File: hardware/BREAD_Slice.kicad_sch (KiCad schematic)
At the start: 23 parts, among them J1 I2C_01x04, J2 Conn_01x10_Female, J3 Screw_Terminal_01x02, J4 Screw_Terminal_01x02, J5 Screw_Terminal_01x06, J6 Screw_Terminal_01x06, SW1 ESTOP, SW2 ESTOP

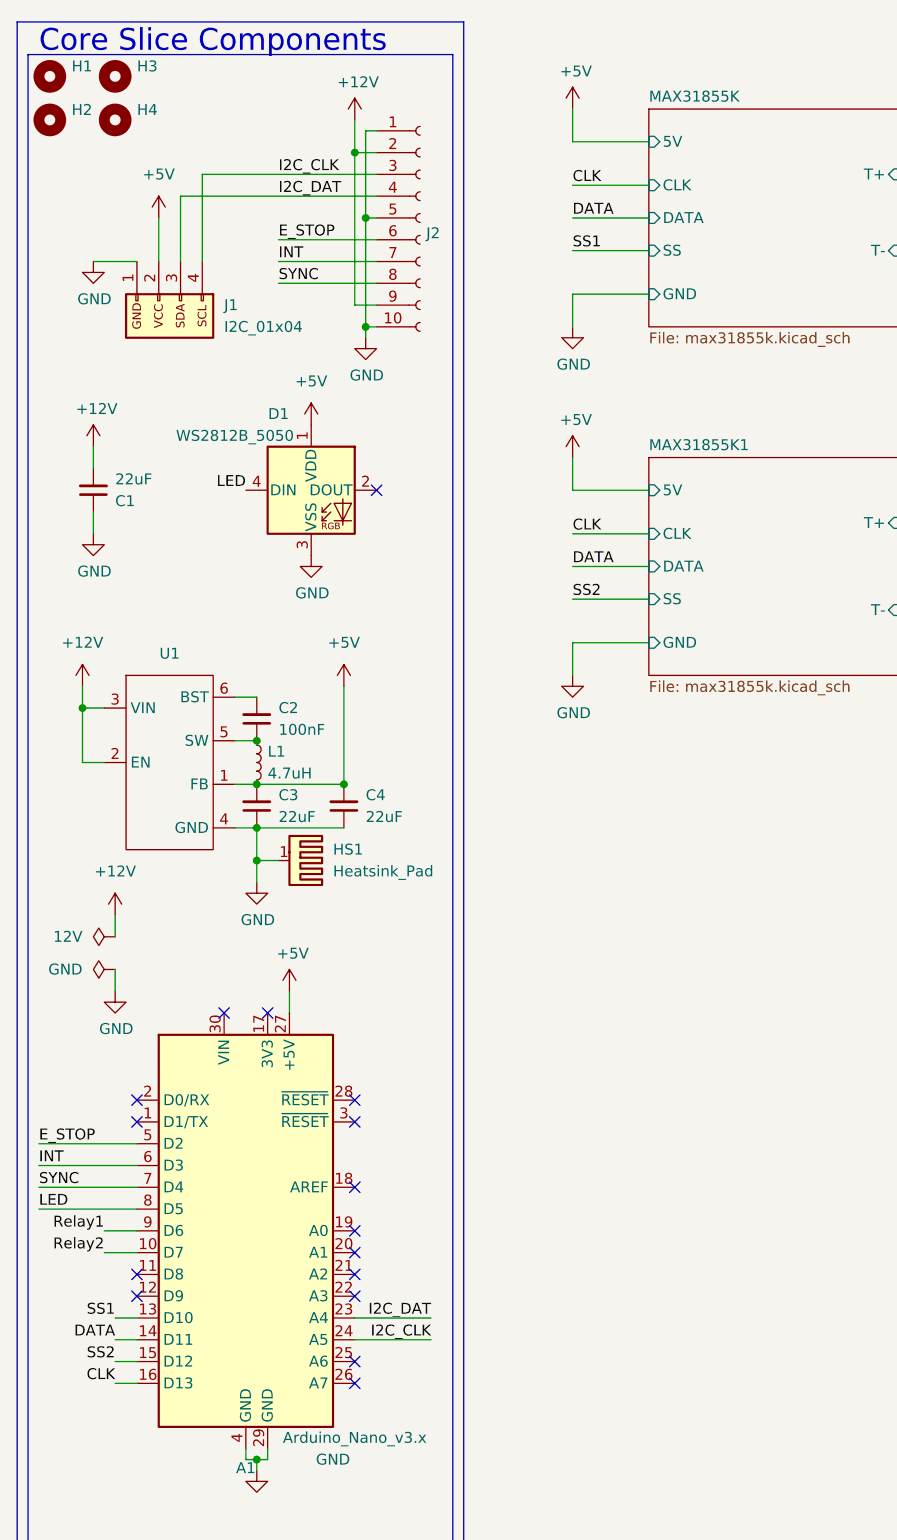
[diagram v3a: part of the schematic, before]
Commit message: added historical scripts and new revisions
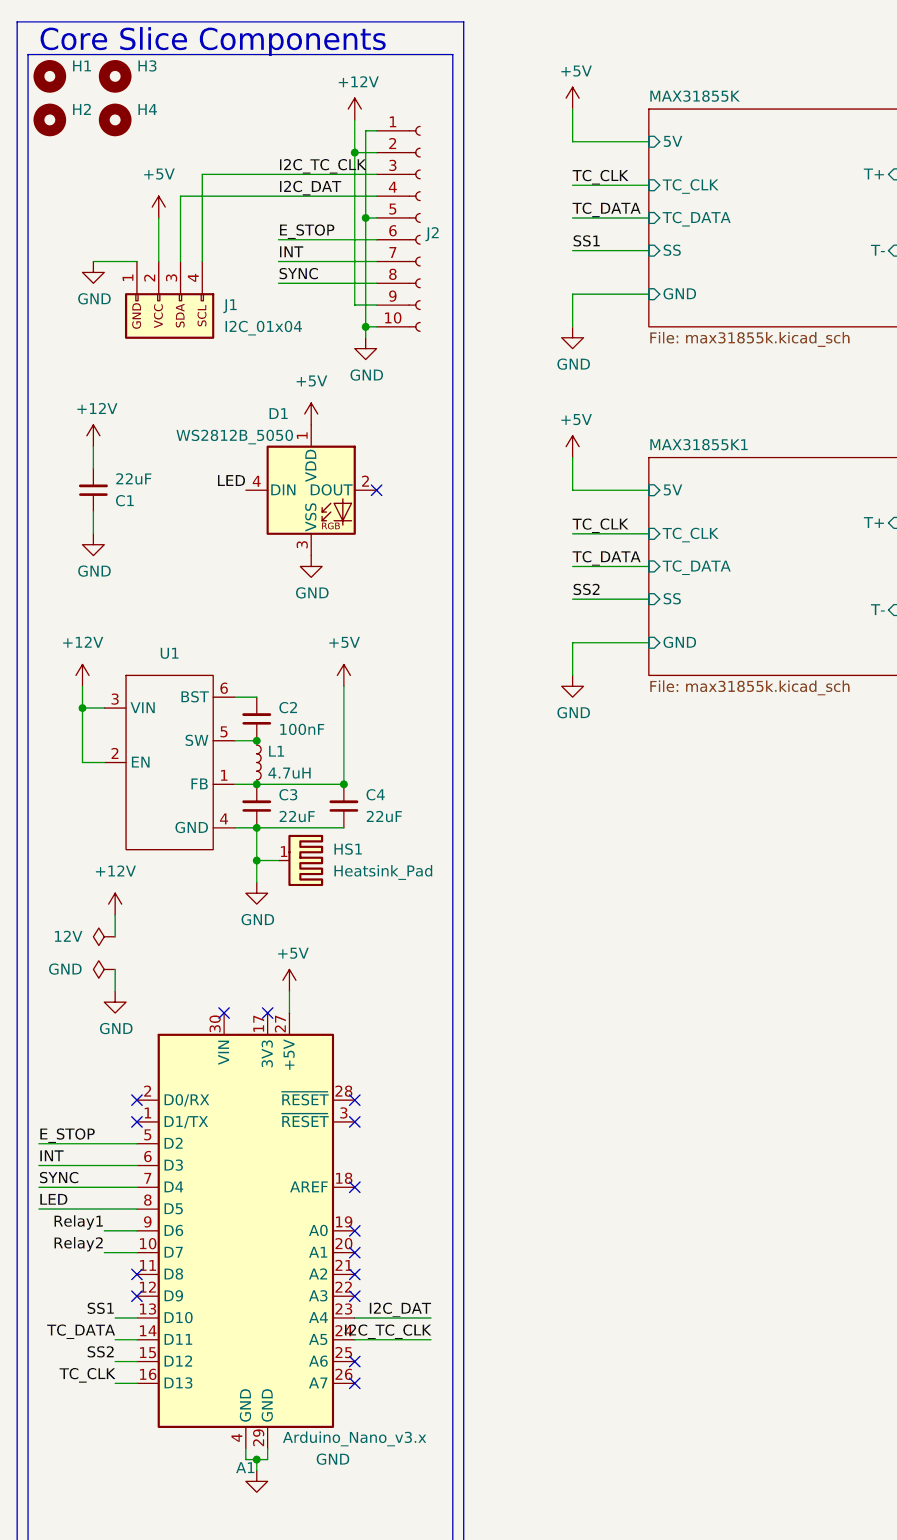
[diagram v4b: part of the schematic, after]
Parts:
- A1: TC_DATAsheet (none) -> http://www.mouser.com/pdfdocs/Gravitech_Arduino_Nano3_0.pdf
- D1: TC_DATAsheet (none) -> https://cdn.sparkfun.com/TC_DATAsheets/BreakoutBoards/WS281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
- F1, F2: TC_DATAsheet (none) -> https://www.digikey.com/short/q7wbwz
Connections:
- net CLK renamed TC_CLK
- net DATA renamed TC_DATA
- net I2C_CLK renamed I2C_TC_CLK
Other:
- sheet MAX31855K ports: added TC_CLK, TC_DATA; removed CLK, DATA
- sheet MAX31855K1 ports: added TC_CLK, TC_DATA; removed CLK, DATA
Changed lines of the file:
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@@
 		)
 	)
-	(label "CLK"
+	(label "TC_CLK"
 		(at 78.74 33.02 0)
 		(fields_autoplaced yes)
@@
 		)
 	)
-	(label "I2C_CLK"
+	(label "I2C_TC_CLK"
 		(at 44.45 31.75 0)
 		(fields_autoplaced yes)
@@
 		)
 	)
-	(label "CLK"
+	(label "TC_CLK"
 		(at 78.74 73.66 0)
 		(fields_autoplaced yes)
@@
 		)
 	)
-	(label "DATA"
+	(label "TC_DATA"
 		(at 78.74 77.47 0)
 		(fields_autoplaced yes)
@@
 		)
 	)
-	(label "CLK"
+	(label "TC_CLK"
 		(at 25.4 172.72 180)
 		(fields_autoplaced yes)
@@
 		)
 	)
-	(label "DATA"
+	(label "TC_DATA"
 		(at 78.74 36.83 0)
 		(fields_autoplaced yes)
@@
 		)
 	)
-	(label "DATA"
+	(label "TC_DATA"
 		(at 25.4 167.64 180)
 		(fields_autoplaced yes)
@@
 		)
 	)
-	(label "I2C_CLK"
+	(label "I2C_TC_CLK"
 		(at 62.23 167.64 180)
 		(fields_autoplaced yes)
@@
 			)
 		)
-		(property "Datasheet" ""
+		(property "TC_DATAsheet" ""
 			(at 41.91 182.88 0)
 			(effects
@@
 			)
 		)
-		(property "Datasheet" ""
+		(property "TC_DATAsheet" ""
 			(at 45.72 127 0)
 			(effects
@@
 			)
 		)
-		(property "Datasheet" ""
+		(property "TC_DATAsheet" ""
 			(at 22.86 73.66 0)
 			(effects
@@
 			)
 		)
-		(property "Datasheet" "~"
+		(property "TC_DATAsheet" "~"
 			(at 17.78 20.32 0)
 			(effects
@@
 			)
 		)
-		(property "Datasheet" "~"
+		(property "TC_DATAsheet" "~"
 			(at 17.78 25.4 0)
 			(effects
@@
 			)
 		)
-		(property "Datasheet" "~"
+		(property "TC_DATAsheet" "~"
 			(at 25.4 20.32 0)
 			(effects
@@
 			)
 		)
-		(property "Datasheet" "~"
+		(property "TC_DATAsheet" "~"
 			(at 25.4 25.4 0)
 			(effects
@@
 			)
 		)
-		(property "Datasheet" "http://www.mouser.com/pdfdocs/Gravitech_Arduino_Nano3_0.pdf"
+		(property "TC_DATAsheet" "http://www.mouser.com/pdfdocs/Gravitech_Arduino_Nano3_0.pdf"
 			(at 40.64 154.94 0)
 			(effects
@@
 			)
 		)
-		(property "Datasheet" "~"
+		(property "TC_DATAsheet" "~"
 			(at 278.13 173.99 0)
 			(effects
@@
 			)
 		)
-		(property "Datasheet" "~"
+		(property "TC_DATAsheet" "~"
 			(at 60.96 36.83 0)
 			(effects
@@
 			)
 		)
-		(property "Datasheet" ""
+		(property "TC_DATAsheet" ""
 			(at 53.34 25.4 0)
 			(effects
@@
 			)
 		)
-		(property "Datasheet" ""
+		(property "TC_DATAsheet" ""
 			(at 54.61 50.8 0)
 			(effects
@@
 			)
 		)
-		(property "Datasheet" ""
+		(property "TC_DATAsheet" ""
 			(at 22.86 63.5 0)
 			(effects
@@
 			)
 		)
-		(property "Datasheet" ""
+		(property "TC_DATAsheet" ""
 			(at 78.74 49.53 0)
 			(effects
@@
 			)
 		)
-		(property "Datasheet" ""
+		(property "TC_DATAsheet" ""
 			(at 25.4 118.11 0)
 			(effects
@@
 			)
 		)
-		(property "Datasheet" ""
+		(property "TC_DATAsheet" ""
 			(at 78.74 24.13 0)
 			(effects
@@
 			)
 		)
-		(property "Datasheet" "~"
+		(property "TC_DATAsheet" "~"
 			(at 25.4 120.65 0)
 			(effects
@@
 			)
 		)
-		(property "Datasheet" ""
+		(property "TC_DATAsheet" ""
 			(at 157.48 59.69 0)
 			(effects
@@
 			)
 		)
-		(property "Datasheet" ""
+		(property "TC_DATAsheet" ""
 			(at 205.74 50.8 0)
 			(effects
@@
 			)
 		)
-		(property "Datasheet" "~"
+		(property "TC_DATAsheet" "~"
 			(at 41.91 95.25 0)
 			(effects
@@
 			)
 		)
-		(property "Datasheet" ""
+		(property "TC_DATAsheet" ""
 			(at 21.59 91.44 0)
 			(effects
@@
 			)
 		)
-		(property "Datasheet" "~"
+		(property "TC_DATAsheet" "~"
 			(at 214.63 48.26 0)
 			(effects
@@
 			)
 		)
-		(property "Datasheet" "~"
+		(property "TC_DATAsheet" "~"
 			(at 41.91 105.41 0)
 			(effects
@@
 			)
 		)
-		(property "Datasheet" "~"
+		(property "TC_DATAsheet" "~"
 			(at 210.82 96.52 0)
 			(effects
@@
 			)
 		)
-		(property "Datasheet" "~"
+		(property "TC_DATAsheet" "~"
 			(at 222.25 96.52 0)
 			(effects
@@
 			)
 		)
-		(property "Datasheet" ""
+		(property "TC_DATAsheet" ""
 			(at 31.75 96.52 0)
 			(effects
@@
 			)
 		)
-		(property "Datasheet" "https://www.digikey.com/short/q7wbwz"
+		(property "TC_DATAsheet" "https://www.digikey.com/short/q7wbwz"
 			(at 195.58 110.49 0)
 			(effects
@@
 			)
 		)
-		(property "Datasheet" ""
+		(property "TC_DATAsheet" ""
 			(at 25.4 127 0)
 			(effects
@@
 			)
 		)
-		(property "Datasheet" "~"
+		(property "TC_DATAsheet" "~"
 			(at 226.06 48.26 0)
 			(effects
@@
 			)
 		)
-		(property "Datasheet" ""
+		(property "TC_DATAsheet" ""
 			(at 41.91 114.3 0)
 			(effects
@@
 			)
 		)
-		(property "Datasheet" ""
+		(property "TC_DATAsheet" ""
 			(at 78.74 64.77 0)
 			(effects
@@
 			)
 		)
-		(property "Datasheet" "~"
+		(property "TC_DATAsheet" "~"
 			(at 45.72 112.0648 0)
 			(effects
@@
 			)
 		)
-		(property "Datasheet" "~"
+		(property "TC_DATAsheet" "~"
 			(at 132.08 76.2 0)
 			(effects
@@
 			)
 		)
-		(property "Datasheet" ""
+		(property "TC_DATAsheet" ""
 			(at 153.67 88.9 0)
 			(effects
@@
 			)
 		)
-		(property "Datasheet" "~"
+		(property "TC_DATAsheet" "~"
 			(at 25.4 124.46 0)
 			(effects
@@
 			)
 		)
-		(property "Datasheet" "~"
+		(property "TC_DATAsheet" "~"
 			(at 41.91 100.33 0)
 			(effects
@@
 			)
 		)
-		(property "Datasheet" ""
+		(property "TC_DATAsheet" ""
 			(at 78.74 90.17 0)
 			(effects
@@
 			)
 		)
-		(property "Datasheet" ""
+		(property "TC_DATAsheet" ""
 			(at 30.48 36.83 0)
 			(effects
@@
 			)
 		)
-		(property "Datasheet" ""
+		(property "TC_DATAsheet" ""
 			(at 153.67 107.95 0)
 			(effects
@@
 			)
 		)
-		(property "Datasheet" ""
+		(property "TC_DATAsheet" ""
 			(at 48.26 76.2 0)
 			(effects
@@
 			)
 		)
-		(property "Datasheet" ""
+		(property "TC_DATAsheet" ""
 			(at 52.07 91.44 0)
 			(effects
@@
 			)
 		)
-		(property "Datasheet" "~"
+		(property "TC_DATAsheet" "~"
 			(at 52.07 105.41 0)
 			(effects
@@
 			)
 		)
-		(property "Datasheet" ""
+		(property "TC_DATAsheet" ""
 			(at 201.93 99.06 0)
 			(effects
@@
 			)
 		)
-		(property "Datasheet" ""
+		(property "TC_DATAsheet" ""
 			(at 22.86 41.91 0)
 			(effects
@@
 			)
 		)
-		(property "Datasheet" "https://www.digikey.com/short/q7wbwz"
+		(property "TC_DATAsheet" "https://www.digikey.com/short/q7wbwz"
 			(at 199.39 62.23 0)
 			(effects
@@
 			)
 		)
-		(property "Datasheet" ""
+		(property "TC_DATAsheet" ""
 			(at 48.26 60.96 0)
 			(effects
@@
 			)
 		)
-		(property "Datasheet" "~"
+		(property "TC_DATAsheet" "~"
 			(at 130.81 35.56 0)
 			(effects
@@
 			)
 		)
-		(property "Datasheet" "https://cdn.sparkfun.com/datasheets/BreakoutBoards/WS2812B.pdf"
+		(property "TC_DATAsheet" "https://cdn.sparkfun.com/TC_DATAsheets/BreakoutBoards/WS2812B.pdf"
 			(at 50.8 78.105 0)
 			(effects
@@
 			)
 		)
-		(property "Datasheet" ""
+		(property "TC_DATAsheet" ""
 			(at 157.48 40.64 0)
 			(effects
@@
 			)
 		)
-		(property "Datasheet" "~"
+		(property "TC_DATAsheet" "~"
 			(at 22.86 68.58 0)
 			(effects
@@
 			)
 		)
-		(property "Datasheet" "~"
+		(property "TC_DATAsheet" "~"
 			(at 33.02 49.53 0)
 			(effects
@@
 			)
 		)
-		(pin "CLK" input
+		(pin "TC_CLK" input
 			(at 87.63 33.02 180)
 			(effects
@@
 			)
 		)
-		(pin "DATA" input
+		(pin "TC_DATA" input
 			(at 87.63 36.83 180)
 			(effects
@@
 			)
 		)
-		(pin "CLK" input
+		(pin "TC_CLK" input
 			(at 87.63 73.66 180)
 			(effects
@@
 			)
 		)
-		(pin "DATA" input
+		(pin "TC_DATA" input
 			(at 87.63 77.47 180)
 			(effects

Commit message: review and revise for current template and kmlib; still needs updating
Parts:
- removed F1, F2: 10A, Fuse:Fuseholder_Clip-5x20mm_Bel_FC-203-22_Lateral_P17.80x5.00mm_D1.17mm_Horizontal, symbol OCI_UPL_11_Mechanical:FUSE_Blade
- removed J1: I2C_01x04, Connector_JST:JST_SH_SM04B-SRSS-TB_1x04-1MP_P1.00mm_Horizontal, symbol SparkFun-Connector:I2C_01x04
- added F1, F2: Fuse, Fuse:Fuseholder_Clip-5x20mm_Bel_FC-203-22_Lateral_P17.80x5.00mm_D1.17mm_Horizontal, symbol Device:Fuse
- D1: footprint SparkFun-LED:WS2812-5050-4PIN -> KMLib_IC_SMD:WS2812-5050-4PIN; PROD_ID (none) -> DIO-12503
- HS1: footprint KML-Custom:Thermal Pad -> KMLib_Mounting:Thermal Pad
- J1: renamed from J2; symbol Connector:Conn_01x10_Female -> Connector:Conn_01x10_Socket
- U1: footprint Package_TO_SOT_SMD:TSOT-23-6 -> KMLib_IC_SMD:SOIC_05WU-7_DIO; symbol SparkFun-DiscreteSemi:AP63205 -> KMLib_IC_Power:AP63205WU-7_Buck_Regulator
- renumbered J3 to J2, J4 to J3, J5 to J4, J6 to J5
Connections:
- net GND: now also J4.3 (Pin_3), J5.3 (Pin_3); no longer J4.4 (Pin_4), J5.4 (Pin_4)
- net MAX31855K/T+: now also J2.2 (Pin_2); no longer J2.1 (Pin_1)
- net MAX31855K/T-: now also J2.1 (Pin_1); no longer J2.2 (Pin_2)
- net MAX31855K1/T+: now also J3.2 (Pin_2); no longer J3.1 (Pin_1)
- net MAX31855K1/T-: now also J3.1 (Pin_1); no longer J3.2 (Pin_2)
- net Relay/IN: now also F1.1
- net Relay/NC: now also J4.6 (Pin_6); no longer J4.1 (Pin_1)
- net Relay/NO: now also J4.5 (Pin_5); no longer J4.2 (Pin_2)
- net Relay1/IN: now also F2.1
- net Relay1/NC: now also J5.6 (Pin_6); no longer J5.1 (Pin_1)
- net Relay1/NO: now also J5.5 (Pin_5); no longer J5.2 (Pin_2)
- net SS1: now also A1.16 (D13); no longer A1.13 (D10)
- net SS2: now also A1.14 (D11); no longer A1.15 (D12)
- net TC_CLK: now also A1.13 (D10); no longer A1.16 (D13)
- net TC_DATA: now also A1.15 (D12); no longer A1.14 (D11)
- net at SW1.2 (B): now also J4.1 (Pin_1), F1.2; no longer J4.6 (Pin_6)
- net at SW2.2 (B): now also J5.1 (Pin_1), F2.2; no longer J5.6 (Pin_6)
- new net: J4.2 (Pin_2), J4.4 (Pin_4), SW1.1 (A)
- new net: J5.2 (Pin_2), J5.4 (Pin_4), SW2.1 (A)
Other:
- note added: "FIXME: THIS NEEDS UPDATING TO THE V1 NANO TEMPLATE MOST RECENT"
- moved on the sheet: J5, SW2
